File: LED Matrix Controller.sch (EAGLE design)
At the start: 8 parts, among them J1 5V PWR, J2 LED OUT, J3 AVR ISP, J4 SER DBG, U1 328P

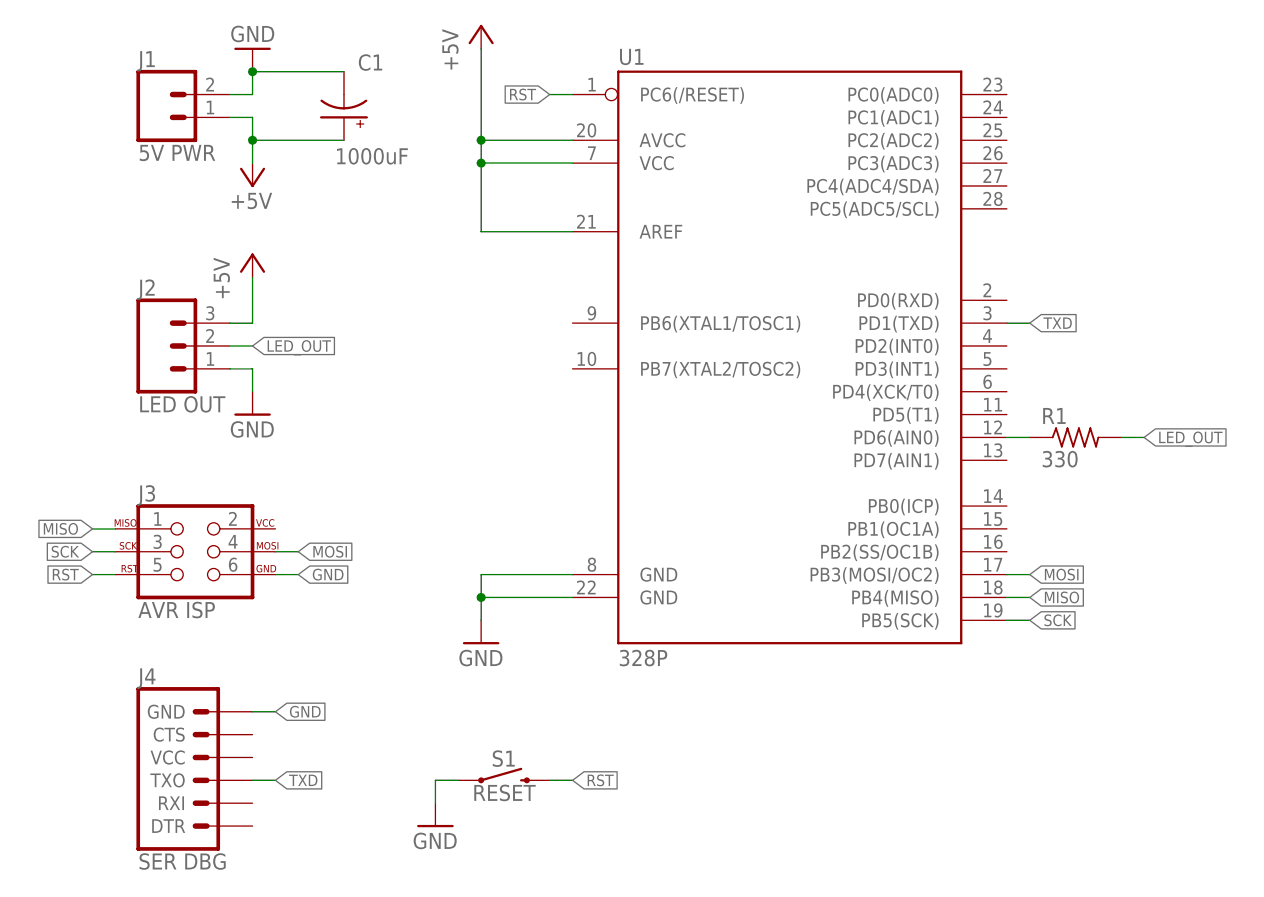
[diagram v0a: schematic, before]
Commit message: Replace ATmega328P with ESP32 dev board
Quick and dirty routing to stick a DOIT ESP32 dev module on the
board. No attention given to RF keepout.
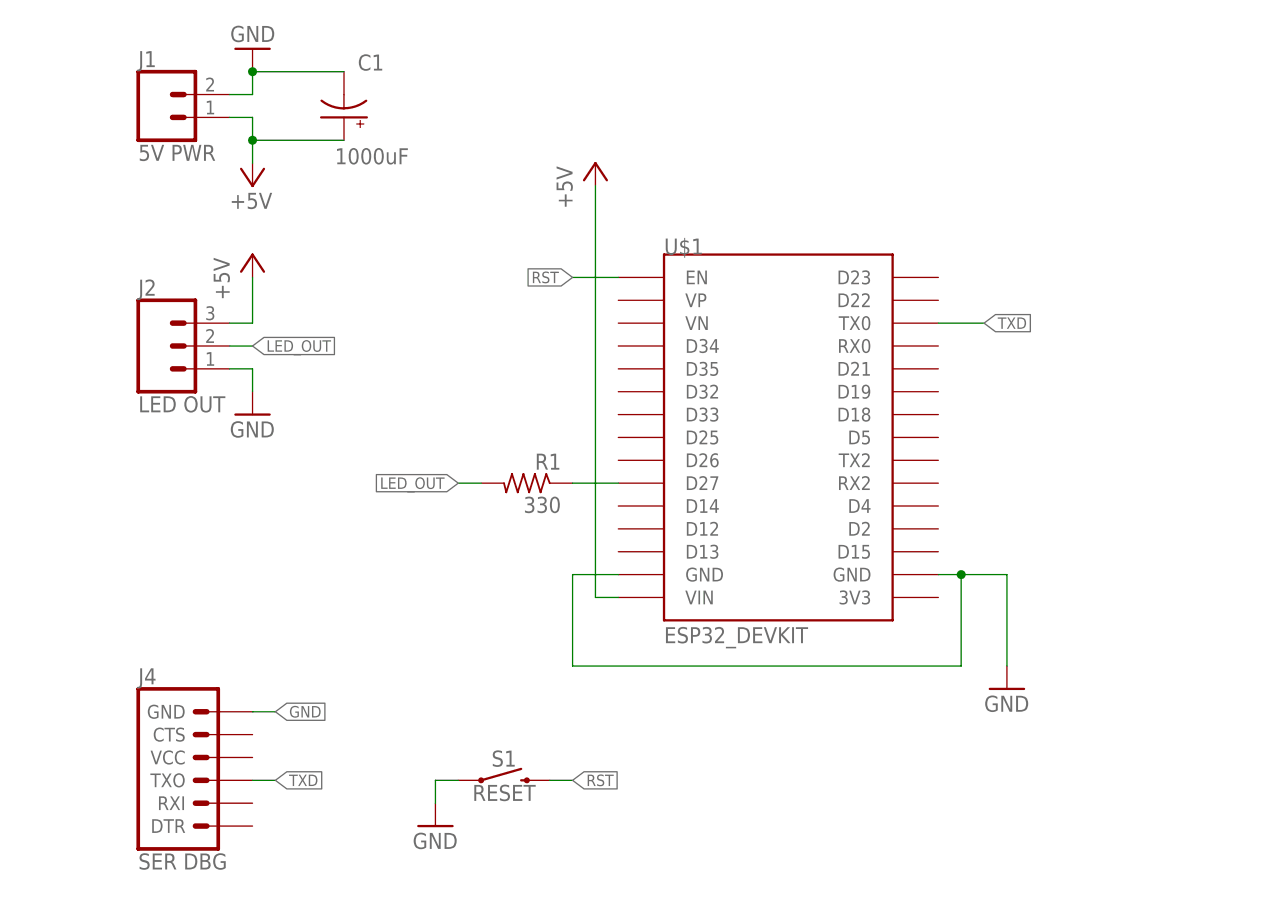
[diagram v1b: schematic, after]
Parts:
- removed J3: AVR ISP, SparkFun-Connectors:AVR_SPI_PROG_3X2PTH
- removed U1: 328P, SparkFun-IC-Microcontroller:ATMEGA328P_PDIP
- added U$1: ESP32_DEVKIT, DOIT_ESP32_DEVKIT:ESP32_DEVKIT
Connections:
- removed net MISO: J3.1, U1.PB4(MISO)
- removed net MOSI: J3.4, U1.PB3(MOSI/OC2)
- removed net SCK: J3.3, U1.PB5(SCK)
- net +5V: now also U$1.VIN; no longer U1.AREF, U1.AVCC, U1.VCC
- net GND: now also U$1.GND@1, U$1.GND@2; no longer J3.6, U1.GND@1, U1.GND@2
- net N$1: now also U$1.D27; no longer U1.PD6(AIN0)
- net RST: now also U$1.EN; no longer J3.5, U1.PC6(/RESET)
- net TXD: now also U$1.TX0; no longer U1.PD1(TXD)
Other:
- moved on the sheet: R1
